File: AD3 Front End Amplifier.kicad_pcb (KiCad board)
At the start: 4 copper layers, 72.4 x 65.4 mm, 50 parts, among them IC101 XC6901D501MR-G, J101 CH1, J102 CH2, J103 W1, J104 W2, J105 Conn_01x15_Pin, J106 Conn_01x15_Socket, J107 Conn_01x15_Pin, J108 Conn_01x15_Socket, SW101 AC/DC, SW102 AC/DC, SW103 50, SW104 50, U101 MIC5504-2.5YM5, U102 OPA356xxDBV, U103 OPA356xxDBV, U104 OPA356xxDBV, U105 OPA356xxDBV

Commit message: v2 gerbers and pdf schematics
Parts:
- removed C101, C102, C109, C110, C111, C112, C113, C114, C115, C116: 10u, Capacitor_SMD:C_0603_1608Metric_Pad1.08x0.95mm_HandSolder
- removed C105, C106: 10n, Capacitor_THT:C_Rect_L7.0mm_W2.5mm_P5.00mm
- removed C107, C108: 1u, Capacitor_SMD:C_0603_1608Metric_Pad1.08x0.95mm_HandSolder
- removed IC101: XC6901D501MR-G, XC6901:SOT95P280X130-5N
- removed J101: CH1, Connector_Coaxial:BNC_Amphenol_B6252HB-NPP3G-50_Horizontal
- removed J102: CH2, Connector_Coaxial:BNC_Amphenol_B6252HB-NPP3G-50_Horizontal
- removed R102, R103: 1M, Resistor_SMD:R_0805_2012Metric_Pad1.20x1.40mm_HandSolder
- removed R104, R105: 100, Resistor_SMD:R_0402_1005Metric_Pad0.72x0.64mm_HandSolder
- removed R106, R107, R109, R111, R112, R113: 402, Resistor_SMD:R_0402_1005Metric_Pad0.72x0.64mm_HandSolder
- removed R108, R110, R114, R115: 22, Resistor_SMD:R_0402_1005Metric_Pad0.72x0.64mm_HandSolder
- removed R116: 49.9, Resistor_SMD:R_0603_1608Metric_Pad0.98x0.95mm_HandSolder
- removed the REF** at (96.3, 95.8)
- removed the REF** at (99.6, 146.8)
- removed SW101, SW102: AC/DC, Button_Switch_THT:SW_DIP_SPSTx01_Slide_9.78x4.72mm_W7.62mm_P2.54mm
- removed SW103, SW104: 50, Button_Switch_THT:SW_DIP_SPSTx01_Slide_9.78x4.72mm_W7.62mm_P2.54mm
- removed U101: MIC5504-2.5YM5, Package_TO_SOT_SMD:SOT-23-5
- removed U102, U103, U104: OPA356xxDBV, Package_TO_SOT_SMD:SOT-23-5
- added C117: 1u, Capacitor_SMD:C_0402_1005Metric_Pad0.74x0.62mm_HandSolder, B.Cu at (203.2, 109.3)
- added C118: 1u, Capacitor_SMD:C_0402_1005Metric_Pad0.74x0.62mm_HandSolder, B.Cu at (194.9, 109.3)
- added C119: 1u, Capacitor_SMD:C_0402_1005Metric_Pad0.74x0.62mm_HandSolder, B.Cu at (201.0, 109.2)
- added C120: 1u, Capacitor_SMD:C_0402_1005Metric_Pad0.74x0.62mm_HandSolder, B.Cu at (209.8, 109.2)
- added C121: 1u, Capacitor_SMD:C_0402_1005Metric_Pad0.74x0.62mm_HandSolder, B.Cu at (196.3, 120.4)
- added C122: 1u, Capacitor_SMD:C_0402_1005Metric_Pad0.74x0.62mm_HandSolder, B.Cu at (196.3, 114.6)
- added C123: 1u, Capacitor_SMD:C_0402_1005Metric_Pad0.74x0.62mm_HandSolder, B.Cu at (192.2, 120.4)
- added C124: 1u, Capacitor_SMD:C_0402_1005Metric_Pad0.74x0.62mm_HandSolder, B.Cu at (192.2, 114.6)
- added C201: 10n, Capacitor_SMD:C_0402_1005Metric_Pad0.74x0.62mm_HandSolder, F.Cu at (222.1, 126.5)
- added C202: 10n, Capacitor_SMD:C_0805_2012Metric_Pad1.18x1.45mm_HandSolder, F.Cu at (222.4, 118.2)
- added C203: 1u, Capacitor_SMD:C_0402_1005Metric_Pad0.74x0.62mm_HandSolder, F.Cu at (225.0, 123.8)
- added C204: 1u, Capacitor_SMD:C_0402_1005Metric_Pad0.74x0.62mm_HandSolder, F.Cu at (219.4, 122.5)
- added C205: 1u, Capacitor_SMD:C_0402_1005Metric_Pad0.74x0.62mm_HandSolder, F.Cu at (214.3, 119.7)
- added C206: 1u, Capacitor_SMD:C_0402_1005Metric_Pad0.74x0.62mm_HandSolder, F.Cu at (210.3, 121.7)
- added C207: 1u, Capacitor_SMD:C_0402_1005Metric_Pad0.74x0.62mm_HandSolder, F.Cu at (211.3, 125.8)
- added C208: 1u, Capacitor_SMD:C_0402_1005Metric_Pad0.74x0.62mm_HandSolder, F.Cu at (214.8, 122.2)
- added C301: 10n, Capacitor_SMD:C_0402_1005Metric_Pad0.74x0.62mm_HandSolder, F.Cu at (222.2, 99.5)
- added C302: 10n, Capacitor_SMD:C_0805_2012Metric_Pad1.18x1.45mm_HandSolder, F.Cu at (222.5, 91.1)
- added C303: 1u, Capacitor_SMD:C_0402_1005Metric_Pad0.74x0.62mm_HandSolder, F.Cu at (225.0, 96.8)
- added C304: 1u, Capacitor_SMD:C_0402_1005Metric_Pad0.74x0.62mm_HandSolder, F.Cu at (219.4, 95.5)
- added C305: 1u, Capacitor_SMD:C_0402_1005Metric_Pad0.74x0.62mm_HandSolder, F.Cu at (214.4, 92.7)
- added C306: 1u, Capacitor_SMD:C_0402_1005Metric_Pad0.74x0.62mm_HandSolder, F.Cu at (210.3, 94.7)
- added C307: 1u, Capacitor_SMD:C_0402_1005Metric_Pad0.74x0.62mm_HandSolder, F.Cu at (211.3, 98.8)
- added C308: 1u, Capacitor_SMD:C_0402_1005Metric_Pad0.74x0.62mm_HandSolder, F.Cu at (214.9, 95.2)
- added D201: D_TVS, Diode_SMD:D_0402_1005Metric_Pad0.77x0.64mm_HandSolder, F.Cu at (226.5, 118.7)
- added D301: D_TVS, Diode_SMD:D_0402_1005Metric_Pad0.77x0.64mm_HandSolder, F.Cu at (226.6, 91.6)
- added FB101: FerriteBead_Small, Inductor_SMD:L_0603_1608Metric_Pad1.05x0.95mm_HandSolder, B.Cu at (196.8, 117.5)
- added FB102: FerriteBead_Small, Inductor_SMD:L_0603_1608Metric_Pad1.05x0.95mm_HandSolder, B.Cu at (192.8, 117.5)
- added H201: SMS-409F, SMS409:SMS409F, F.Cu at (215.5, 122.0)
- added H301: SMS-409F, SMS409:SMS409F, F.Cu at (215.6, 95.0)
- added IC103: XC6901D501MR-G, XC6901:SOT95P280X130-5N, B.Cu at (206.5, 108.7)
- added IC201: TS12A4516DBVR, TS12A4516:SOT95P280X145-5N, F.Cu at (222.2, 123.2)
- added IC301: TS12A4516DBVR, TS12A4516:SOT95P280X145-5N, F.Cu at (222.2, 96.2)
- added J201: CH1, Connector_Coaxial:BNC_Amphenol_B6252HB-NPP3G-50_Horizontal, F.Cu at (236.2, 118.9)
- added J301: CH1, Connector_Coaxial:BNC_Amphenol_B6252HB-NPP3G-50_Horizontal, F.Cu at (236.3, 91.8)
- added R118: 49.9, Resistor_SMD:R_0603_1608Metric_Pad0.98x0.95mm_HandSolder, F.Cu at (182.9, 83.0)
- added R201: 1k, Resistor_SMD:R_0402_1005Metric_Pad0.72x0.64mm_HandSolder, F.Cu at (222.1, 127.8)
- added R202: 1M, Resistor_SMD:R_0805_2012Metric_Pad1.20x1.40mm_HandSolder, F.Cu at (217.9, 119.2)
- added R203: 100, Resistor_SMD:R_0402_1005Metric_Pad0.72x0.64mm_HandSolder, F.Cu at (206.6, 118.7)
- added R204: 402, Resistor_SMD:R_0402_1005Metric_Pad0.72x0.64mm_HandSolder, F.Cu at (207.7, 118.7)
- added R205: 22, Resistor_SMD:R_0402_1005Metric_Pad0.72x0.64mm_HandSolder, F.Cu at (210.7, 123.0)
- added R206: 402, Resistor_SMD:R_0402_1005Metric_Pad0.72x0.64mm_HandSolder, F.Cu at (217.9, 122.8)
- added R207: 402, Resistor_SMD:R_0402_1005Metric_Pad0.72x0.64mm_HandSolder, F.Cu at (217.9, 125.5)
- added R208: 22, Resistor_SMD:R_0402_1005Metric_Pad0.72x0.64mm_HandSolder, F.Cu at (209.1, 124.3)
- added R301: 1k, Resistor_SMD:R_0402_1005Metric_Pad0.72x0.64mm_HandSolder, F.Cu at (222.2, 100.8)
- added R302: 1M, Resistor_SMD:R_0805_2012Metric_Pad1.20x1.40mm_HandSolder, F.Cu at (217.9, 92.2)
- added R303: 100, Resistor_SMD:R_0402_1005Metric_Pad0.72x0.64mm_HandSolder, F.Cu at (206.7, 91.7)
- added R304: 402, Resistor_SMD:R_0402_1005Metric_Pad0.72x0.64mm_HandSolder, F.Cu at (207.8, 91.6)
- added R305: 22, Resistor_SMD:R_0402_1005Metric_Pad0.72x0.64mm_HandSolder, F.Cu at (210.7, 96.0)
- added R306: 402, Resistor_SMD:R_0402_1005Metric_Pad0.72x0.64mm_HandSolder, F.Cu at (217.9, 95.8)
- added R307: 402, Resistor_SMD:R_0402_1005Metric_Pad0.72x0.64mm_HandSolder, F.Cu at (217.9, 98.5)
- added R308: 22, Resistor_SMD:R_0402_1005Metric_Pad0.72x0.64mm_HandSolder, F.Cu at (209.2, 97.2)
- added REF**: OSHW-Logo2_7.3x6mm_SilkScreen, Symbol:OSHW-Logo2_7.3x6mm_SilkScreen, B.Cu at (197.2, 76.1)
- added REF**: KiCad-Logo2_5mm_SilkScreen, Symbol:KiCad-Logo2_5mm_SilkScreen, B.Cu at (224.2, 76.3)
- added SW201: AC/DC, Button_Switch_THT:SW_DIP_SPSTx01_Slide_9.78x4.72mm_W7.62mm_P2.54mm, F.Cu at (192.0, 123.7)
- added SW301: AC/DC, Button_Switch_THT:SW_DIP_SPSTx01_Slide_9.78x4.72mm_W7.62mm_P2.54mm, F.Cu at (192.0, 103.7)
- added U201: OPA356xxDBV, Package_TO_SOT_SMD:SOT-23-5, F.Cu at (211.0, 118.9)
- added U202: OPA356xxDBV, Package_TO_SOT_SMD:SOT-23-5, F.Cu at (214.6, 125.0)
- added U301: OPA356xxDBV, Package_TO_SOT_SMD:SOT-23-5, F.Cu at (211.1, 91.9)
- added U302: OPA356xxDBV, Package_TO_SOT_SMD:SOT-23-5, F.Cu at (214.6, 98.0)
- U105: value OPA356xxDBV -> MIC5504-2.5YM5; moved to B.Cu
- moved R117 120.8 mm to (230.7, 80.8), turned to 180 degrees
- moved J103 105.4 mm to (241.3, 76.2)
- moved J107 102.0 mm to (229.9, 69.2), turned to -90 degrees
- moved J105 101.9 mm to (229.9, 66.7), turned to -90 degrees
- moved J108 86.4 mm to (180.3, 131.3)
- moved J106 86.4 mm to (177.8, 131.3)
- moved J104 76.3 mm to (182.9, 76.2)
- moved U105 75.9 mm to (198.1, 108.7), turned to 0 degrees
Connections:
- net /V+ renamed /V+_CONN
- net /V- renamed /V-_CONN
- J106 pad 1: /CH1_OUT- -> CH1_OUT-
- J106 pad 2: /CH2_OUT- -> CH2_OUT-
- J108 pad 1: /CH1_OUT+ -> CH1_OUT+
- J108 pad 2: /CH2_OUT+ -> CH2_OUT+
- R117 pad 1: Net-(J104-In) -> Net-(J103-In)
- R117 pad 2: /W2 -> /W1
- U105 pad 1: Net-(R113-Pad1) -> V+
- U105 pad 2: -2V5 -> GND
- U105 pad 3: GND -> V+
- U105 pad 4: Net-(U105--) -> unconnected-(U105-NC-Pad4)
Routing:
- net V+: track 0.00 -> 123.8 mm, vias 0 -> 4
- net V-: track 0.00 -> 86.2 mm, vias 0 -> 2
- net /CH2_OUT-: track 65.0 -> 0.00 mm
- net /CH2_OUT+: track 56.3 -> 0.00 mm
- net CH2_OUT-: track 0.00 -> 56.2 mm
- net CH2_OUT+: track 0.00 -> 54.7 mm
- net Net-(IC301-IN): track 0.00 -> 42.2 mm
- net /D14: track 80.7 -> 40.5 mm
- net /D6: track 75.3 -> 35.9 mm
- net Net-(IC201-IN): track 0.00 -> 37.9 mm
- net /D15: track 72.1 -> 35.9 mm
- net +2V5: track 104.9 -> 69.6 mm, vias 4 -> 6
- net CH1_OUT-: track 0.00 -> 34.6 mm
- net /W1: track 52.2 -> 85.7 mm
- net /D5: track 73.0 -> 39.5 mm
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- added copper zone on F.Cu, net GND
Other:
- board size 72.4 x 65.4 mm -> 75.9 x 74.6 mm
- board text added: "AD3 Low Noise Amplifier v0.2"
- board text added: "CH1"
- board text added: "CH2"
- board text added: "DIGITAL"
- board text added: "GND"
- board text added: "PSU"
- board text added: "TRIG"
- board text added: "W1"
- board text added: "W2"
- board text removed: "Analog Discovery Front End Amplifier v0.1"
- board text removed: "Warning: Power Supply MAX +-5V"

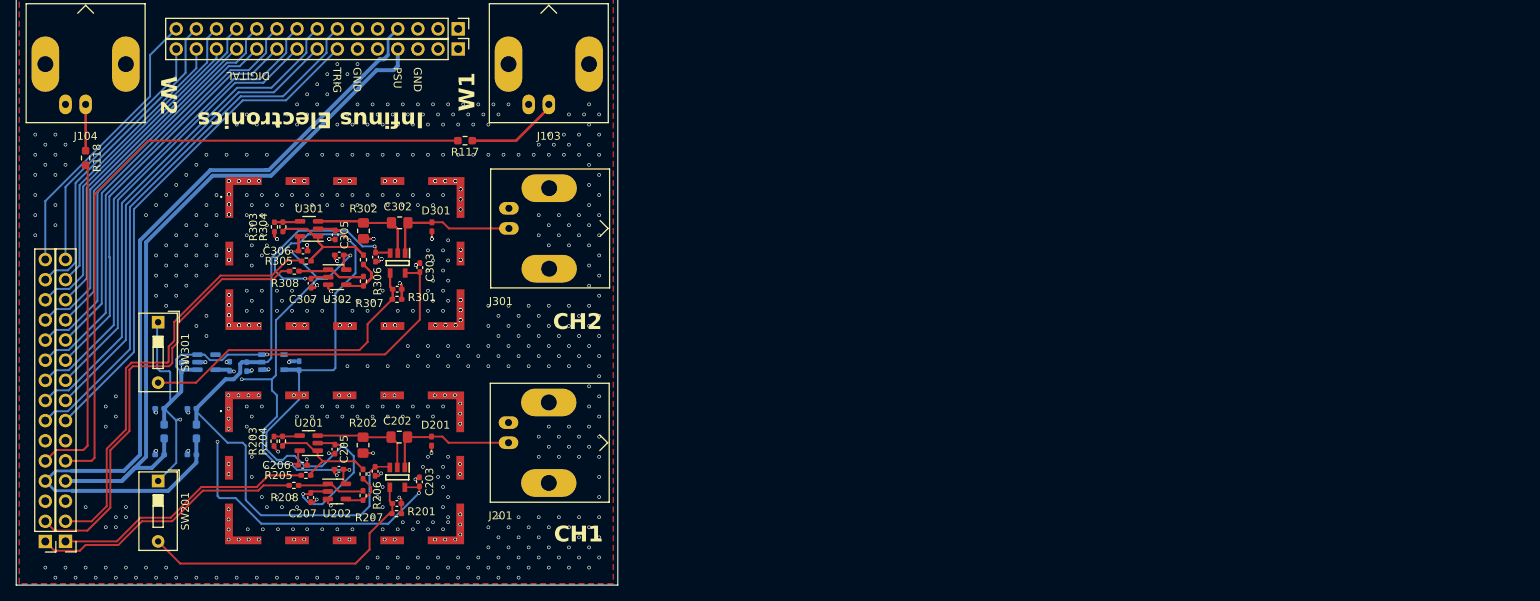
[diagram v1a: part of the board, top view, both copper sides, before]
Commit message: Ch1 Layout
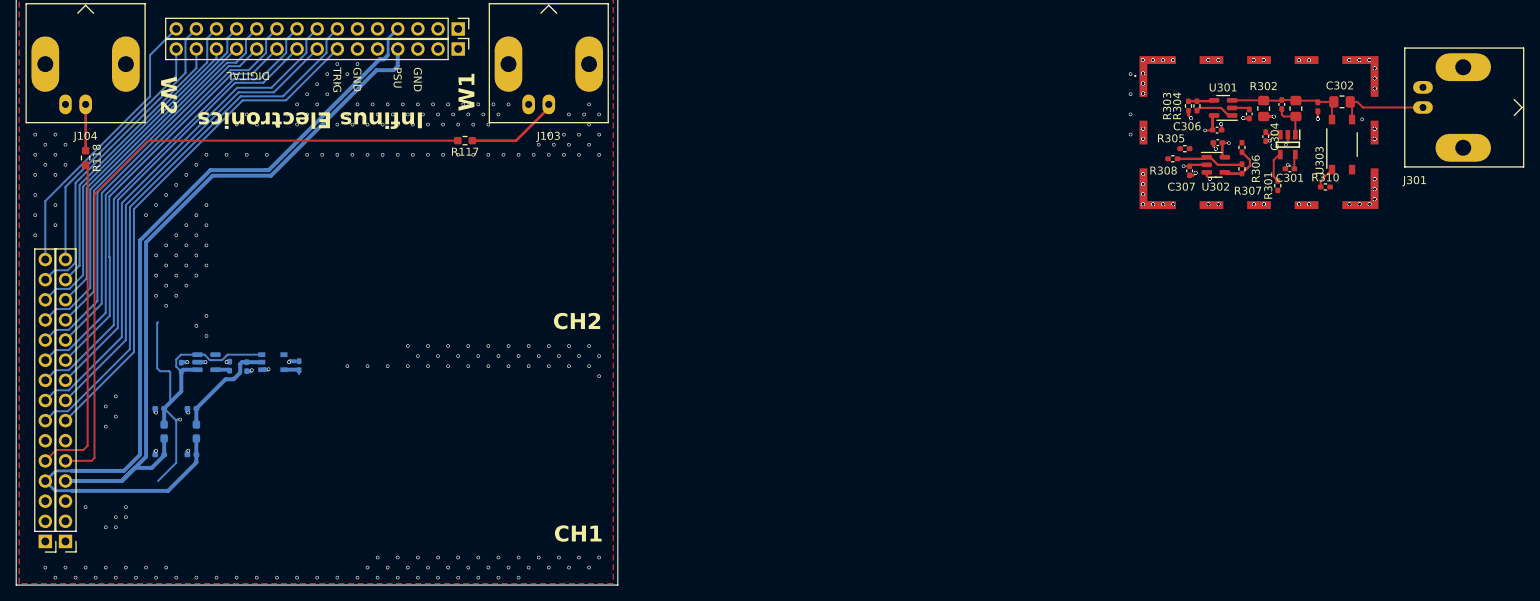
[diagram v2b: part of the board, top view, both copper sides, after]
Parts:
- removed C201: 10n, Capacitor_SMD:C_0402_1005Metric_Pad0.74x0.62mm_HandSolder
- removed C202: 10n, Capacitor_SMD:C_0805_2012Metric_Pad1.18x1.45mm_HandSolder
- removed C203, C204, C205, C206, C207, C208: 1u, Capacitor_SMD:C_0402_1005Metric_Pad0.74x0.62mm_HandSolder
- removed D201: D_TVS, Diode_SMD:D_0402_1005Metric_Pad0.77x0.64mm_HandSolder
- removed H201: SMS-409F, SMS409:SMS409F
- removed IC201: TS12A4516DBVR, TS12A4516:SOT95P280X145-5N
- removed J201: CH1, Connector_Coaxial:BNC_Amphenol_B6252HB-NPP3G-50_Horizontal
- removed R201: 1k, Resistor_SMD:R_0402_1005Metric_Pad0.72x0.64mm_HandSolder
- removed R202: 1M, Resistor_SMD:R_0805_2012Metric_Pad1.20x1.40mm_HandSolder
- removed R203: 100, Resistor_SMD:R_0402_1005Metric_Pad0.72x0.64mm_HandSolder
- removed R204, R206, R207: 402, Resistor_SMD:R_0402_1005Metric_Pad0.72x0.64mm_HandSolder
- removed R205, R208: 22, Resistor_SMD:R_0402_1005Metric_Pad0.72x0.64mm_HandSolder
- removed REF**: OSHW-Logo2_7.3x6mm_SilkScreen, Symbol:OSHW-Logo2_7.3x6mm_SilkScreen
- removed REF**: KiCad-Logo2_5mm_SilkScreen, Symbol:KiCad-Logo2_5mm_SilkScreen
- removed SW201, SW301: AC/DC, Button_Switch_THT:SW_DIP_SPSTx01_Slide_9.78x4.72mm_W7.62mm_P2.54mm
- removed U201, U202: OPA356xxDBV, Package_TO_SOT_SMD:SOT-23-5
- added R309: 100k, Resistor_SMD:R_0805_2012Metric_Pad1.20x1.40mm_HandSolder, F.Cu at (335.5, 76.7)
- added R310: 402, Resistor_SMD:R_0402_1005Metric_Pad0.72x0.64mm_HandSolder, F.Cu at (339.3, 86.6)
- added U303: TLP176AM, Package_SO:MFSOP6-4_4.4x3.6mm_P1.27mm, F.Cu at (341.4, 81.3)
- C301: value 10n -> 1u
- C303: value 1u -> 270p
- moved C302 119.8 mm to (341.4, 75.9)
- moved C305 116.3 mm to (329.7, 77.4)
- moved C306 116.3 mm to (325.6, 79.4)
- moved H301 116.3 mm to (330.9, 79.8)
- moved U301 116.3 mm to (326.4, 76.6)
- moved J301 116.3 mm to (351.6, 76.6)
- moved R303 116.3 mm to (322.0, 76.4)
- moved R304 116.3 mm to (323.1, 76.4)
- moved R302 114.6 mm to (331.5, 76.7)
- moved C301 113.6 mm to (334.8, 84.3), turned to 180 degrees
- moved C304 113.3 mm to (331.7, 80.3)
- moved IC301 113.3 mm to (334.5, 81.3)
- moved D301 112.8 mm to (338.3, 76.5)
- moved R301 112.0 mm to (333.2, 86.4), turned to 90 degrees
- moved U302 111.7 mm to (325.4, 83.8)
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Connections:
- C301 pad 1: Net-(IC301-IN) -> V+
- C302 pad 1: Net-(D301-A2) -> Net-(J301-In)
- C302 pad 2: Net-(IC301-NO) -> Net-(D301-A2)
- C303 pad 1: V+ -> Net-(D301-A2)
- C303 pad 2: GND -> Net-(IC301-COM)
- IC301 pad 1: Net-(D301-A2) -> Net-(IC301-COM)
- IC301 pad 2: Net-(IC301-NO) -> GND
- J301 pad 1: Net-(D301-A2) -> Net-(J301-In)
- R301 pad 1: Net-(IC301-IN) -> Net-(SW302-A)
- R301 pad 2: GND -> Net-(IC301-IN)
- R302 pad 1: Net-(IC301-NO) -> Net-(D301-A2)
- U301 pad 3: Net-(IC301-NO) -> Net-(D301-A2)
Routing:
- net -2V5: track 96.6 -> 12.2 mm, vias 4 -> 1
- net V-: track 86.2 -> 14.8 mm, vias 2 -> 0
- net V+: track 123.8 -> 56.1 mm, vias 4 -> 1
- net +2V5: track 69.6 -> 11.0 mm, vias 6 -> 2
- net CH2_OUT-: track 56.2 -> 0.00 mm
- net CH2_OUT+: track 54.7 -> 0.00 mm
- net Net-(IC301-IN): track 42.2 -> 3.96 mm
- net Net-(IC201-IN): track 37.9 -> 0.00 mm
- net CH1_OUT-: track 34.6 -> 0.00 mm
- net CH1_OUT+: track 33.2 -> 0.00 mm
- net Net-(IC301-NO): track 28.0 -> 0.00 mm
- net Net-(R304-Pad2): track 29.0 -> 9.95 mm
- net Net-(D201-A2): track 17.1 -> 0.00 mm
- net GND: track 39.8 -> 24.1 mm, vias 639 -> 352
- net Net-(R204-Pad2): track 14.5 -> 0.00 mm
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
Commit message: v3 done
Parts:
- added C201: 10n, Capacitor_SMD:C_0805_2012Metric_Pad1.18x1.45mm_HandSolder, F.Cu at (227.6, 118.7)
- added C202: 270p, Capacitor_SMD:C_0402_1005Metric_Pad0.74x0.62mm_HandSolder, F.Cu at (220.7, 119.1)
- added C203: 1u, Capacitor_SMD:C_0402_1005Metric_Pad0.74x0.62mm_HandSolder, F.Cu at (218.0, 123.1)
- added C204: 1u, Capacitor_SMD:C_0402_1005Metric_Pad0.74x0.62mm_HandSolder, F.Cu at (221.0, 127.2)
- added C205: 1u, Capacitor_SMD:C_0402_1005Metric_Pad0.74x0.62mm_HandSolder, F.Cu at (215.9, 120.2)
- added C206: 1u, Capacitor_SMD:C_0402_1005Metric_Pad0.74x0.62mm_HandSolder, F.Cu at (211.8, 122.3)
- added C207: 1u, Capacitor_SMD:C_0402_1005Metric_Pad0.74x0.62mm_HandSolder, F.Cu at (208.4, 127.4)
- added C208: 1u, Capacitor_SMD:C_0402_1005Metric_Pad0.74x0.62mm_HandSolder, F.Cu at (211.9, 123.9)
- added C209: (select on test), Capacitor_SMD:C_0402_1005Metric_Pad0.74x0.62mm_HandSolder, F.Cu at (219.5, 119.1)
- added C309: (select on test), Capacitor_SMD:C_0402_1005Metric_Pad0.74x0.62mm_HandSolder, F.Cu at (219.5, 93.1)
- added D201: D_TVS, Diode_SMD:D_0402_1005Metric_Pad0.77x0.64mm_HandSolder, F.Cu at (224.5, 119.3)
- added H201: SMS-409F, SMS409:SMS409F, F.Cu at (217.1, 122.6)
- added IC201: TS12A4516DBVR, TS12A4516:SOT95P280X145-5N, F.Cu at (220.8, 124.1)
- added J201: CH1, Connector_Coaxial:BNC_Amphenol_B6252HB-NPP3G-50_Horizontal, F.Cu at (237.8, 119.4)
- added R201: 402, Resistor_SMD:R_0402_1005Metric_Pad0.72x0.64mm_HandSolder, F.Cu at (225.5, 129.5)
- added R202: 1M, Resistor_SMD:R_0805_2012Metric_Pad1.20x1.40mm_HandSolder, F.Cu at (217.7, 119.6)
- added R203: 100k, Resistor_SMD:R_0805_2012Metric_Pad1.20x1.40mm_HandSolder, F.Cu at (222.5, 119.6)
- added R204: 100, Resistor_SMD:R_0402_1005Metric_Pad0.72x0.64mm_HandSolder, F.Cu at (208.2, 119.2)
- added R205: 1k, Resistor_SMD:R_0402_1005Metric_Pad0.72x0.64mm_HandSolder, F.Cu at (219.5, 129.3)
- added R206: 402, Resistor_SMD:R_0402_1005Metric_Pad0.72x0.64mm_HandSolder, F.Cu at (209.3, 119.2)
- added R207: 22, Resistor_SMD:R_0402_1005Metric_Pad0.72x0.64mm_HandSolder, F.Cu at (207.8, 124.6)
- added R208: 402, Resistor_SMD:R_0402_1005Metric_Pad0.72x0.64mm_HandSolder, F.Cu at (215.0, 124.5)
- added R209: 402, Resistor_SMD:R_0402_1005Metric_Pad0.72x0.64mm_HandSolder, F.Cu at (215.0, 127.2)
- added R210: 22, Resistor_SMD:R_0402_1005Metric_Pad0.72x0.64mm_HandSolder, F.Cu at (206.2, 125.9)
- added SW201: AC/DC, Button_Switch_THT:SW_DIP_SPSTx01_Slide_9.78x4.72mm_W7.62mm_P2.54mm, F.Cu at (197.6, 113.3)
- added SW202: /10, Button_Switch_THT:SW_DIP_SPSTx01_Slide_9.78x4.72mm_W7.62mm_P2.54mm, F.Cu at (197.6, 124.8)
- added SW301: AC/DC, Button_Switch_THT:SW_DIP_SPSTx01_Slide_9.78x4.72mm_W7.62mm_P2.54mm, F.Cu at (197.6, 87.4)
- added SW302: /10, Button_Switch_THT:SW_DIP_SPSTx01_Slide_9.78x4.72mm_W7.62mm_P2.54mm, F.Cu at (197.6, 98.7)
- added U201: TLP176AM, Package_SO:MFSOP6-4_4.4x3.6mm_P1.27mm, F.Cu at (227.6, 124.1)
- added U202: OPA356xxDBV, Package_TO_SOT_SMD:SOT-23-5, F.Cu at (212.6, 119.5)
- added U203: OPA356xxDBV, Package_TO_SOT_SMD:SOT-23-5, F.Cu at (211.7, 126.7)
- moved C305 115.1 mm to (215.8, 94.3)
- moved H301 115.1 mm to (217.1, 96.6)
- moved R301 115.1 mm to (225.4, 103.5)
- moved R302 115.1 mm to (217.7, 93.6)
- moved U303 115.1 mm to (211.6, 100.7)
- moved C301 115.1 mm to (227.5, 92.8)
- moved C303 115.1 mm to (217.9, 97.1)
- moved C304 115.1 mm to (221.0, 101.2)
- moved C306 115.1 mm to (211.8, 96.3)
- moved C307 115.1 mm to (208.3, 101.5)
- moved C308 115.1 mm to (211.9, 97.9)
- moved D301 115.1 mm to (224.5, 93.4)
- moved J301 115.1 mm to (237.7, 93.5)
- moved R304 115.1 mm to (208.2, 93.3)
- moved R305 115.1 mm to (219.4, 103.3)
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- renumbered C121 to C101, C123 to C102, C122 to C103, C124 to C104, C117 to C105, C118 to C106, C119 to C107, C120 to C108, C302 to C301, C303 to C302, C304 to C303, C301 to C304, IC103 to IC101, J103 to J101, J104 to J102, J105 to J103, J106 to J104, J107 to J105, J108 to J106, R117 to R101, R118 to R102, R310 to R301, R309 to R303, R303 to R304, R301 to R305, R304 to R306, R305 to R307, R306 to R308, R307 to R309, R308 to R310, U105 to U101, U303 to U301, U301 to U302, U302 to U303
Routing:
- net V+: track 56.1 -> 151.9 mm, vias 1 -> 3
- net V-: track 14.8 -> 83.5 mm, vias 0 -> 4
- net -2V5: track 12.2 -> 69.0 mm, vias 1 -> 4
- net +2V5: track 11.0 -> 67.6 mm, vias 2 -> 7
- net Net-(SW301-B): track 0.00 -> 51.5 mm, vias 0 -> 1
- net CH2_OUT-: track 0.00 -> 49.5 mm
- net CH2_OUT+: track 0.00 -> 48.4 mm
- net Net-(SW201-B): track 0.00 -> 48.0 mm, vias 0 -> 1
- net Net-(SW302-A): track 0.00 -> 39.0 mm, vias 0 -> 1
- net Net-(SW202-A): track 0.00 -> 36.7 mm, vias 0 -> 1
- net CH1_OUT-: track 0.00 -> 31.6 mm
- net CH1_OUT+: track 0.00 -> 30.6 mm
- net GND: track 24.1 -> 44.3 mm, vias 352 -> 640
- net Net-(R206-Pad2): track 0.00 -> 19.1 mm
- net Net-(R209-Pad1): track 0.00 -> 17.3 mm
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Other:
- board size 75.9 x 74.6 mm -> 76.4 x 74.6 mm
- board text added: "AD3 Low Noise Amplifier v0.3"
- board text removed: "AD3 Low Noise Amplifier v0.2"

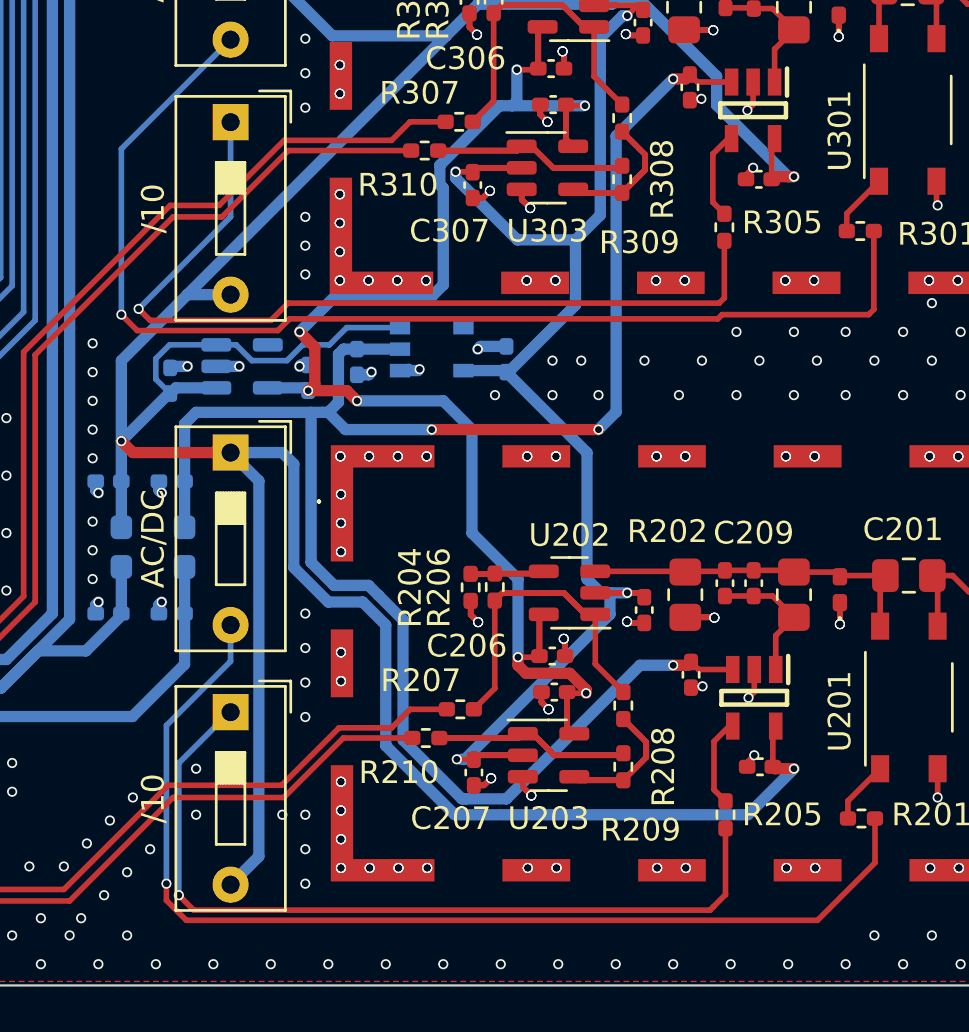
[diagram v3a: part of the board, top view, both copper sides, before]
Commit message: mux in mistake fix
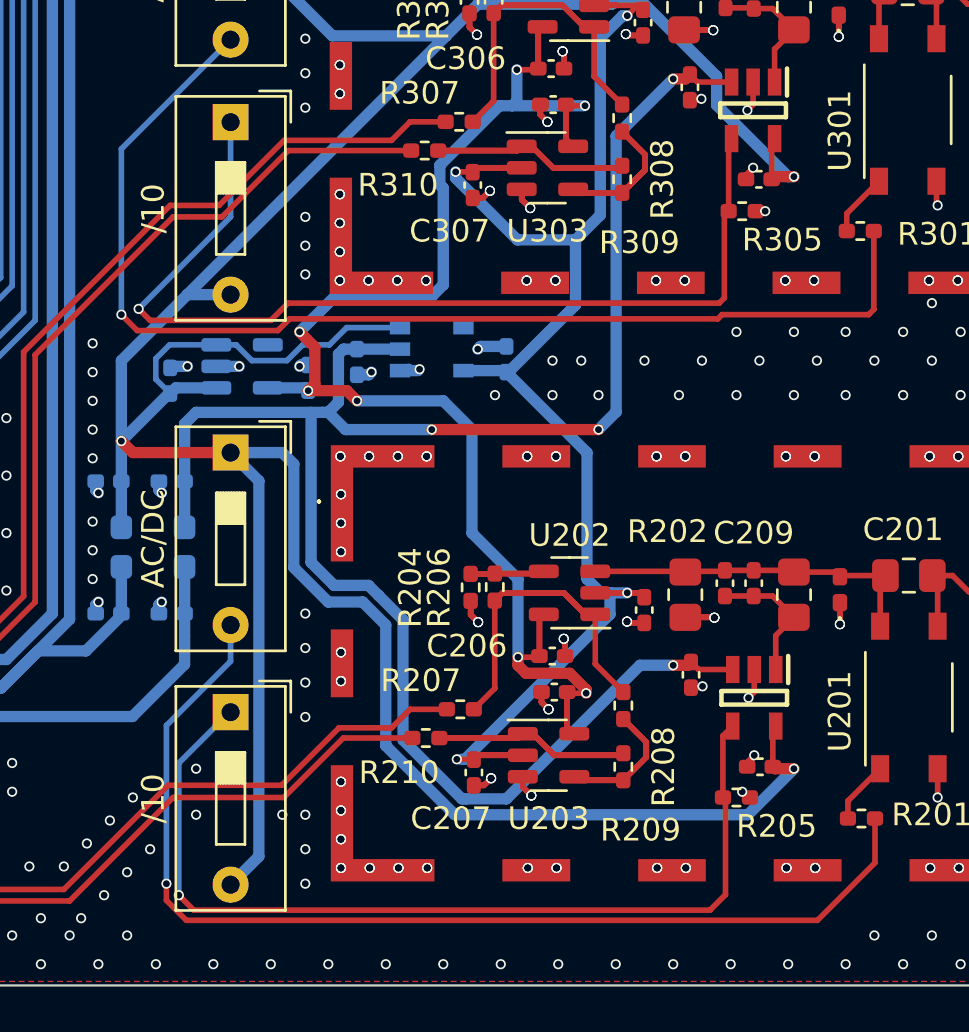
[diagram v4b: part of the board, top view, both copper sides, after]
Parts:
- moved R305 1.06 mm to (220.2, 102.6), turned to 0 degrees
- moved R205 0.90 mm to (220.0, 128.5), turned to 0 degrees
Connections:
- R205 pad 1: Net-(SW202-A) -> Net-(IC201-IN)
- R205 pad 2: Net-(IC201-IN) -> GND
- R305 pad 1: Net-(SW302-A) -> Net-(IC301-IN)
- R305 pad 2: Net-(IC301-IN) -> GND
- SW202 pad 1: Net-(SW202-A) -> Net-(IC201-IN)
- SW302 pad 1: Net-(SW302-A) -> Net-(IC301-IN)
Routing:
- net Net-(IC301-IN): track 3.96 -> 43.8 mm, vias 0 -> 1
- net Net-(SW302-A): track 39.0 -> 0.00 mm, vias 1 -> 0
- net Net-(IC201-IN): track 3.96 -> 41.4 mm, vias 0 -> 1
- net Net-(SW202-A): track 36.7 -> 0.00 mm, vias 1 -> 0
- net GND: track 44.3 -> 45.2 mm, vias 640 -> 642
